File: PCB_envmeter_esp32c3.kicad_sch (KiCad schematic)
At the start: 26 parts, among them J1 USB_C_Receptacle_USB2.0_16P, J2 USB_C_Receptacle_Simple, J3 AE-BME680, J4 SSD1306, SW1 Reset, SW2 Mode, U1 ESP32-C3-WROOM-02, U2 AP7333-33SAG, U3 NJM2845DL1-33

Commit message: Disconnect shield to GND
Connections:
- net GND: no longer J1.S1 (SHIELD), J2.S1 (SHIELD)
- no-connect marks 11 -> 13

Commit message: Change footprint of SW1,2
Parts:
- SW1, SW2: footprint Button_Switch_THT:SW_Tactile_Straight_KSL0Axx1LFTR -> Button_Switch_THT:SW_PUSH_6mm
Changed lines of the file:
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@@
   (title_block
     (title "IoT環境メーター")
-    (date "2024-02-17")
+    (date "2024-02-18")
     (rev "1.1")
     (company "K.Takata")
@@
       (effects (font (size 1.27 1.27)) (justify right))
     )
-    (property "Footprint" "Button_Switch_THT:SW_Tactile_Straight_KSL0Axx1LFTR" (at 205.74 118.11 0)
+    (property "Footprint" "Button_Switch_THT:SW_PUSH_6mm" (at 205.74 118.11 0)
       (effects (font (size 1.27 1.27)) hide)
     )
@@
       (effects (font (size 1.27 1.27)) (justify right))
     )
-    (property "Footprint" "Button_Switch_THT:SW_Tactile_Straight_KSL0Axx1LFTR" (at 124.46 85.09 0)
-      (effects (font (size 1.27 1.27)) hide)
-    )
+    (property "Footprint" "Button_Switch_THT:SW_PUSH_6mm" (at 124.46 85.09 0)
+      (effects (font (size 1.27 1.27)) hide)
+    )

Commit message: Change footprint
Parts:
- removed J2: USB_C_Receptacle_Simple, mylib:Connector_USB_C_simple, symbol mylib:USB_C_Receptacle_Simple
- J1: footprint Connector_USB:USB_C_Receptacle_XKB_U262-16XN-4BVC11 -> mylib:Connector_USB_C_simple_combo
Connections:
- no-connect marks 13 -> 12
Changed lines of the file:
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@@
   (junction (at 66.04 22.86) (diameter 0) (color 0 0 0 0)
-  )
-  (junction (at 59.69 86.36) (diameter 0) (color 0 0 0 0)
-  )
-  (junction (at 58.42 81.28) (diameter 0) (color 0 0 0 0)
-  )
-  (junction (at 60.96 88.9) (diameter 0) (color 0 0 0 0)
   )
   (junction (at 104.14 45.72) (diameter 0) (color 0 0 0 0)
@@
   (no_connect (at 200.66 115.57))
   (no_connect (at 200.66 82.55))
-  (no_connect (at 34.29 172.72))
   (no_connect (at 200.66 105.41))
   (no_connect (at 144.78 87.63))
@@
     (stroke (width 0) (type default))
   )
-  (wire (pts (xy 57.15 81.28) (xy 58.42 81.28))
+  (wire (pts (xy 57.15 81.28) (xy 59.69 81.28))
     (stroke (width 0) (type default))
   )
@@
     (stroke (width 0) (type default))
   )
-  (wire (pts (xy 60.96 142.24) (xy 60.96 88.9))
-    (stroke (width 0) (type default))
-  )
   (wire (pts (xy 59.69 81.28) (xy 59.69 71.12))
     (stroke (width 0) (type default))
   )
-  (wire (pts (xy 62.23 88.9) (xy 60.96 88.9))
-    (stroke (width 0) (type default))
-  )
   (wire (pts (xy 63.5 72.39) (xy 63.5 81.28))
     (stroke (width 0) (type default))
@@
     (stroke (width 0) (type default))
   )
-  (wire (pts (xy 57.15 142.24) (xy 60.96 142.24))
-    (stroke (width 0) (type default))
-  )
   (wire (pts (xy 111.76 143.51) (xy 114.3 143.51))
     (stroke (width 0) (type default))
@@
     (stroke (width 0) (type default))
   )
-  (wire (pts (xy 60.96 147.32) (xy 57.15 147.32))
-    (stroke (width 0) (type default))
-  )
-  (wire (pts (xy 57.15 134.62) (xy 58.42 134.62))
-    (stroke (width 0) (type default))
-  )
   (wire (pts (xy 200.66 102.87) (xy 227.33 102.87))
     (stroke (width 0) (type default))
@@
     (stroke (width 0) (type default))
   )
-  (wire (pts (xy 59.69 86.36) (xy 57.15 86.36))
-    (stroke (width 0) (type default))
-  )
-  (wire (pts (xy 58.42 81.28) (xy 59.69 81.28))
+  (wire (pts (xy 57.15 86.36) (xy 62.23 86.36))
     (stroke (width 0) (type default))
   )
@@
     (stroke (width 0) (type default))
   )
-  (wire (pts (xy 62.23 86.36) (xy 59.69 86.36))
-    (stroke (width 0) (type default))
-  )
   (wire (pts (xy 74.93 90.17) (xy 74.93 88.9))
     (stroke (width 0) (type default))
   )
-  (wire (pts (xy 60.96 149.86) (xy 57.15 149.86))
-    (stroke (width 0) (type default))
-  )
   (wire (pts (xy 110.49 24.13) (xy 110.49 22.86))
     (stroke (width 0) (type default))
@@
     (stroke (width 0) (type default))
   )
-  (wire (pts (xy 58.42 134.62) (xy 58.42 81.28))
-    (stroke (width 0) (type default))
-  )
   (wire (pts (xy 110.49 29.21) (xy 110.49 30.48))
     (stroke (width 0) (type default))
@@
     (stroke (width 0) (type default))
   )
-  (wire (pts (xy 60.96 88.9) (xy 57.15 88.9))
+  (wire (pts (xy 57.15 88.9) (xy 62.23 88.9))
     (stroke (width 0) (type default))
   )
@@
     (stroke (width 0) (type default))
   )
-  (wire (pts (xy 59.69 139.7) (xy 59.69 86.36))
-    (stroke (width 0) (type default))
-  )
   (wire (pts (xy 111.76 170.18) (xy 114.3 170.18))
     (stroke (width 0) (type default))
@@
   )
   (wire (pts (xy 63.5 81.28) (xy 59.69 81.28))
-    (stroke (width 0) (type default))
-  )
-  (wire (pts (xy 57.15 139.7) (xy 59.69 139.7))
     (stroke (width 0) (type default))
   )
@@
     (effects (font (size 1.27 1.27)) (justify left))
     (property "Intersheetrefs" "${INTERSHEET_REFS}" (at 243.8241 102.87 0)
-      (effects (font (size 1.27 1.27)) (justify left) hide)
-    )
-  )
-  (global_label "D+" (shape bidirectional) (at 60.96 149.86 0) (fields_autoplaced)
-    (effects (font (size 1.27 1.27)) (justify left))
-    (property "Intersheetrefs" "${INTERSHEET_REFS}" (at 67.8989 149.86 0)
-      (effects (font (size 1.27 1.27)) (justify left) hide)
-    )
-  )
-  (global_label "D-" (shape bidirectional) (at 60.96 147.32 0) (fields_autoplaced)
-    (effects (font (size 1.27 1.27)) (justify left))
-    (property "Intersheetrefs" "${INTERSHEET_REFS}" (at 67.8989 147.32 0)
       (effects (font (size 1.27 1.27)) (justify left) hide)
     )
@@
     )
   )
-  (symbol (lib_id "power:GND") (at 41.91 172.72 0) (unit 1)
-    (in_bom yes) (on_board yes) (dnp no) (fields_autoplaced)
-    (property "Reference" "#PWR027" (at 41.91 179.07 0)
-      (effects (font (size 1.27 1.27)) hide)
-    )
-    (property "Value" "GND" (at 41.91 177.8 0)
-      (effects (font (size 1.27 1.27)))
-    )
-    (property "Footprint" "" (at 41.91 172.72 0)
-      (effects (font (size 1.27 1.27)) hide)
-    )
-    (property "Datasheet" "" (at 41.91 172.72 0)
-      (effects (font (size 1.27 1.27)) hide)
-    )
-    (pin "1")
-    (instances
-      (project "PCB_envmeter_esp32c3"
-        (path "/e56fcc30-bb74-4f59-a961-89b735db6e9b"
-          (reference "#PWR027") (unit 1)
-        )
-      )
-    )
-  )
   (symbol (lib_id "Connector:USB_C_Receptacle_USB2.0_16P") (at 41.91 96.52 0) (unit 1)
     (in_bom yes) (on_board yes) (dnp no) (fields_autoplaced)
@@
       (effects (font (size 1.27 1.27)))
     )
-    (property "Footprint" "Connector_USB:USB_C_Receptacle_XKB_U262-16XN-4BVC11" (at 45.72 96.52 0)
+    (property "Footprint" "mylib:Connector_USB_C_simple_combo" (at 45.72 96.52 0)
       (effects (font (size 1.27 1.27)) hide)
     )
@@
     )
   )
-  (symbol (lib_id "mylib:USB_C_Receptacle_Simple") (at 41.91 149.86 0) (unit 1)
-    (in_bom yes) (on_board yes) (dnp no) (fields_autoplaced)
-    (property "Reference" "J2" (at 41.91 127 0)
-      (effects (font (size 1.27 1.27)))
-    )
-    (property "Value" "USB_C_Receptacle_Simple" (at 41.91 129.54 0)
-      (effects (font (size 1.27 1.27)))
-    )
-    (property "Footprint" "mylib:Connector_USB_C_simple" (at 45.72 149.86 0)
-      (effects (font (size 1.27 1.27)) hide)
-    )
-    (property "Datasheet" "https://www.usb.org/sites/default/files/documents/usb_type-c.zip" (at 45.72 149.86 0)
-      (effects (font (size 1.27 1.27)) hide)
-    )
-    (pin "S1")
-    (pin "A9")
-    (pin "A12")
-    (pin "5")
-    (pin "B4")
-    (pin "B6")
-    (pin "B9")
-    (pin "B7")
-    (pin "1")
-    (pin "7")
-    (pin "2")
-    (pin "6")
-    (pin "B12")
-    (pin "3")
-    (pin "4")
-    (instances
-      (project "PCB_envmeter_esp32c3"
-        (path "/e56fcc30-bb74-4f59-a961-89b735db6e9b"
-          (reference "J2") (unit 1)
-        )
-      )
-    )
-  )
   (symbol (lib_id "power:+3.3V") (at 172.72 74.93 0) (unit 1)
     (in_bom yes) (on_board yes) (dnp no) (fields_autoplaced)
@@
         )
       )
-    )
-  )
-  (symbol (lib_id "power:GND") (at 45.72 172.72 0) (unit 1)
-    (in_bom yes) (on_board yes) (dnp no) (fields_autoplaced)
-    (property "Reference" "#PWR026" (at 45.72 179.07 0)
-      (effects (font (size 1.27 1.27)) hide)
-    )
-    (property "Value" "GND" (at 45.72 177.8 0)
-      (effects (font (size 1.27 1.27)))
-    )
-    (property "Footprint" "" (at 45.72 172.72 0)
-      (effects (font (size 1.27 1.27)) hide)
-    )
-    (property "Datasheet" "" (at 45.72 172.72 0)
-      (effects (font (size 1.27 1.27)) hide)
-    )
-    (pin "1")
-    (instances
-      (project "PCB_envmeter_esp32c3"
-        (path "/e56fcc30-bb74-4f59-a961-89b735db6e9b"
-          (reference "#PWR026") (unit 1)
-        )
-      )

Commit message: Update F1 footprint
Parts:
- F1: footprint Capacitor_SMD:C_1210_3225Metric_Pad1.33x2.70mm_HandSolder -> Fuse:Fuse_1206_3216Metric_Pad1.42x1.75mm_HandSolder
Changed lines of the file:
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@@
       (effects (font (size 1.27 1.27)) (justify right))
     )
-    (property "Footprint" "Capacitor_SMD:C_1210_3225Metric_Pad1.33x2.70mm_HandSolder" (at 58.42 63.5 0)
+    (property "Footprint" "Fuse:Fuse_1206_3216Metric_Pad1.42x1.75mm_HandSolder" (at 58.42 63.5 0)
       (effects (font (size 1.27 1.27)) (justify left) hide)
     )

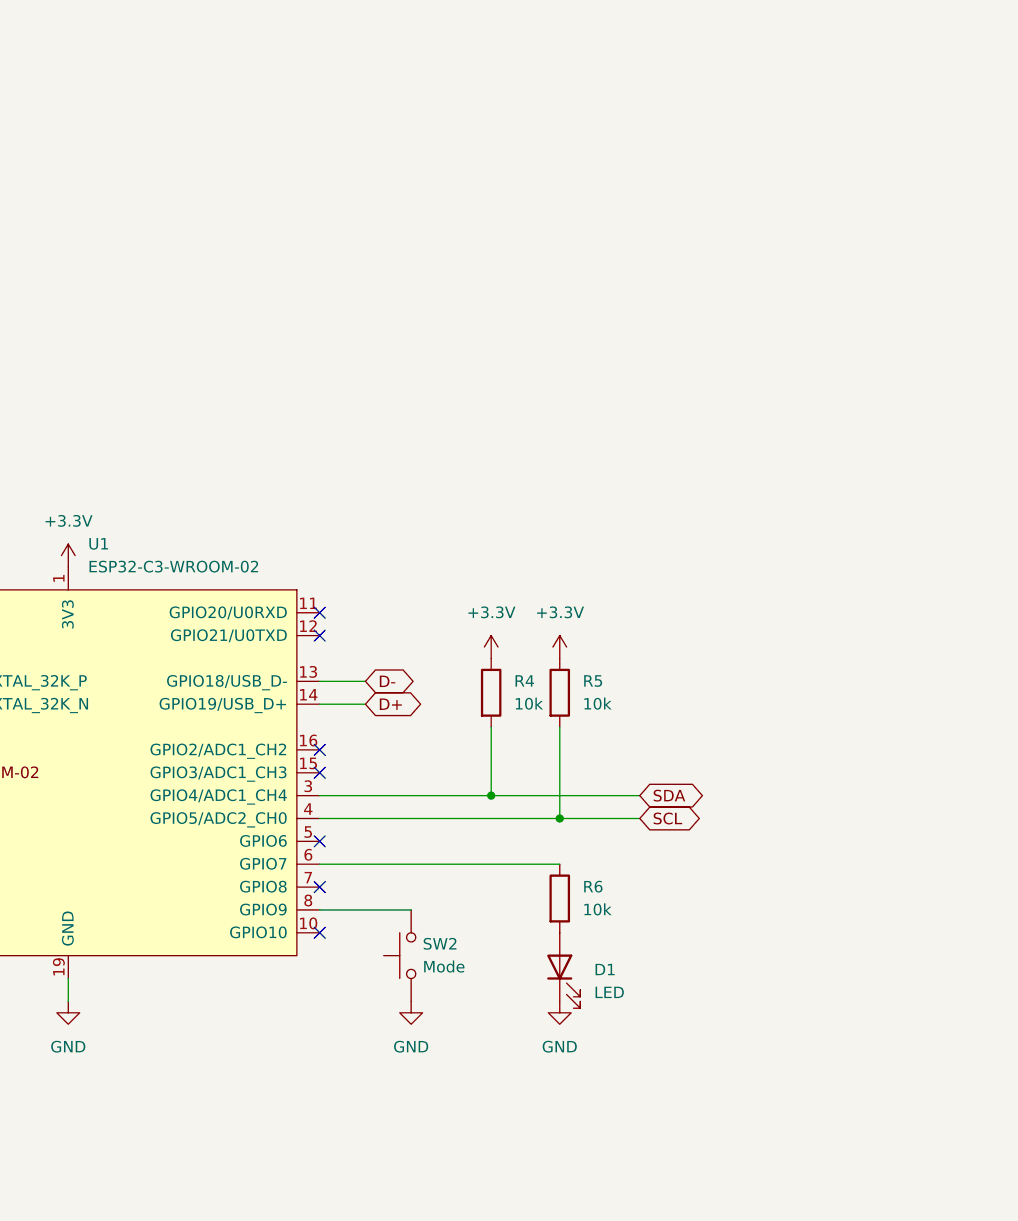
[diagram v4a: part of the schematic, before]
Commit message: Rev. 2
* スマートリモコン機能追加
  - 赤外線送信部
  - 赤外線受信部
* AE-BME680とSSD1306のパッド穴サイズを1.0mmから0.9mmに変更
* JLCJLCJLCJLC を WayWayWay に変更
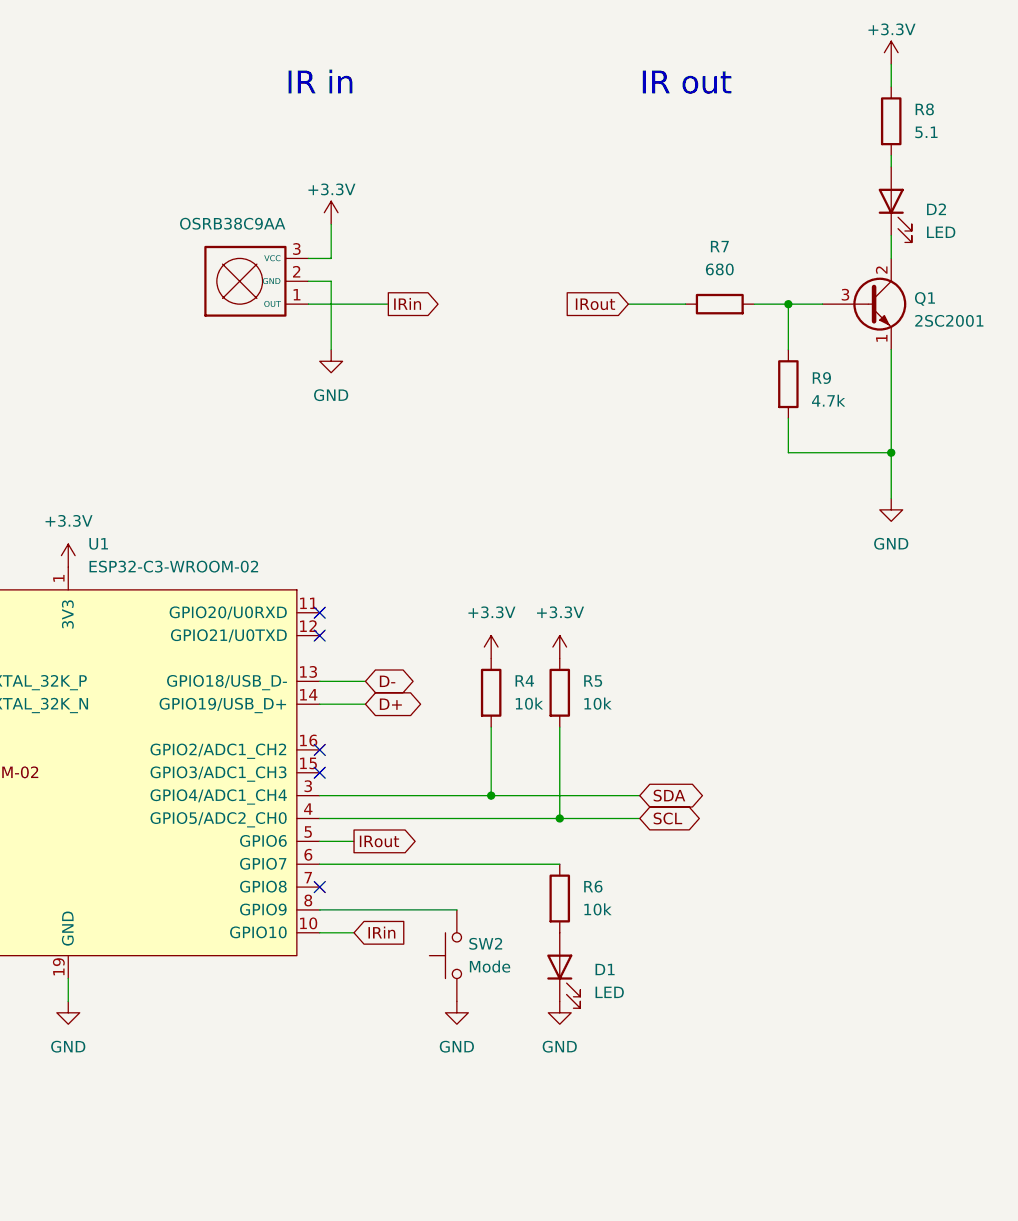
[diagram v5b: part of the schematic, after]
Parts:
- added D2: LED, LED_THT:LED_D5.0mm_IRGrey, symbol Device:LED
- added IRM1: OSRB38C9AA, OptoDevice:Vishay_MINICAST-3Pin, symbol mylib:OSRB38C9AA
- added Q1: 2SC2001, Package_TO_SOT_THT:TO-92_Inline_Wide, symbol Transistor_BJT:2SC1815
- added R7: 680, Resistor_THT:R_Axial_DIN0207_L6.3mm_D2.5mm_P7.62mm_Horizontal, symbol Device:R
- added R8: 5.1, Resistor_THT:R_Axial_DIN0207_L6.3mm_D2.5mm_P7.62mm_Horizontal, symbol Device:R
- added R9: 4.7k, Resistor_THT:R_Axial_DIN0207_L6.3mm_D2.5mm_P7.62mm_Horizontal, symbol Device:R
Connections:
- net +3.3V: now also IRM1.3 (VCC), R8.1
- net GND: now also IRM1.2 (GND), Q1.1 (E), R9.2
- net IRin: now reaches U1.10 (GPIO10)
- net IRin: now also IRM1.1 (OUT)
- net IRout: now reaches U1.5 (GPIO6)
- net IRout: now also R7.1
- new net: D2.2 (A), R8.2
- new net: D2.1 (K), Q1.2 (C)
- new net: Q1.3 (B), R7.2, R9.1
- no-connect marks 12 -> 10
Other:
- note added: "IR in"
- note added: "IR out"
- title: IoT環境メーター -> IoT環境メーター / スマートリモコン
- moved on the sheet: SW2
